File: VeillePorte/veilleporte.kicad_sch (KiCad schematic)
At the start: 0 parts

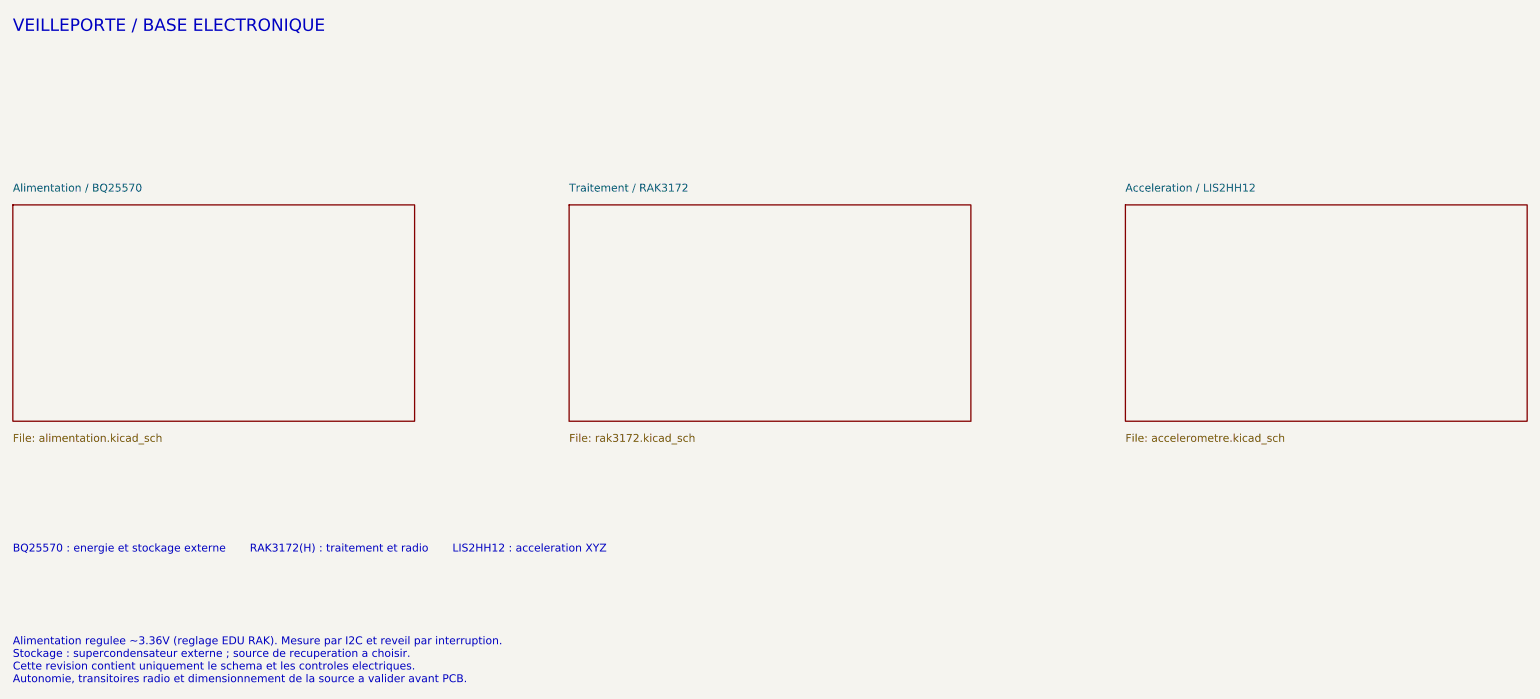
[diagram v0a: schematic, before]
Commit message: Remplace le LIS2HH12 par le raccordement IR VL53L4CD Pololu 3692
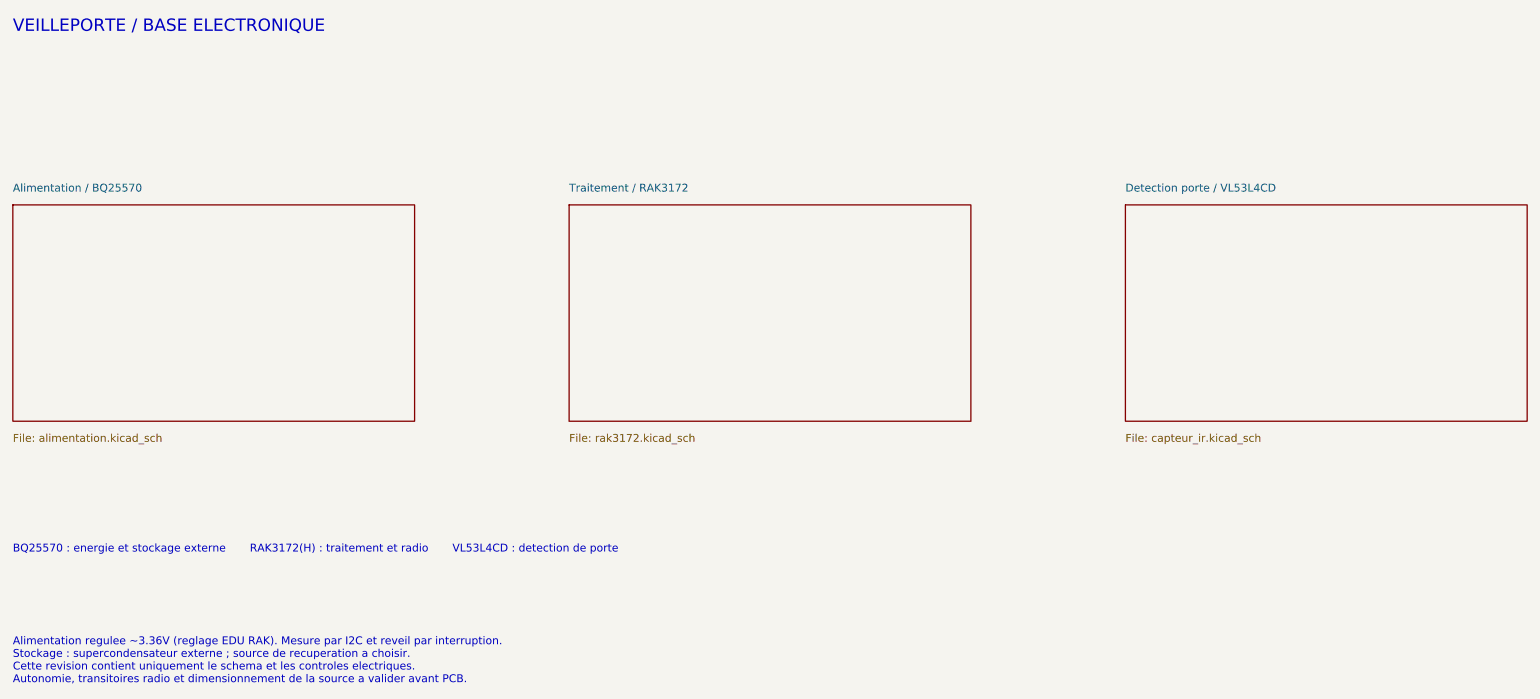
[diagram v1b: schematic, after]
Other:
- sheet Acceleration / LIS2HH12 renamed Detection porte / VL53L4CD
- sheet Detection porte / VL53L4CD: file accelerometre.kicad_sch -> capteur_ir.kicad_sch
- note added: "BQ25570 : energie et stockage externe RAK3172(H) : traitement et radio VL53L4CD : detection de porte"
- note removed: "BQ25570 : energie et stockage externe RAK3172(H) : traitement et radio LIS2HH12 : acceleration XYZ"

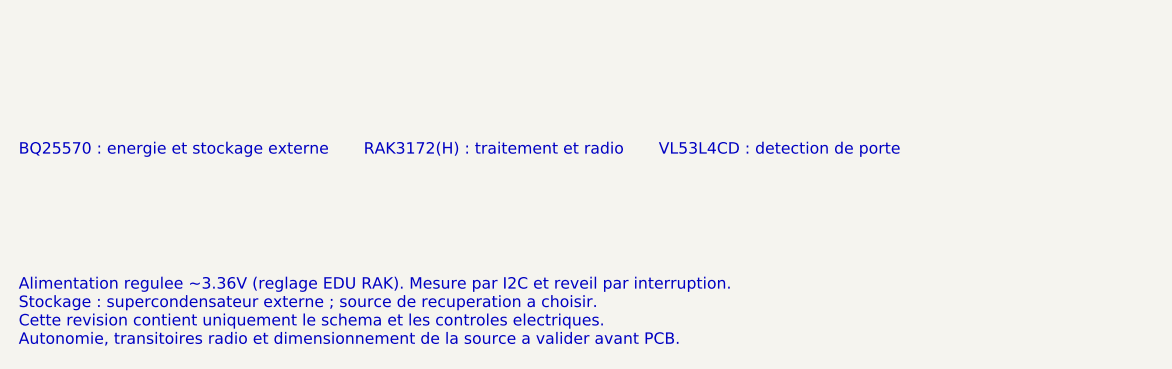
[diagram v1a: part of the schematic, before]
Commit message: Regle le BQ25570 pour supercapacite 4V et structure la feuille RAK
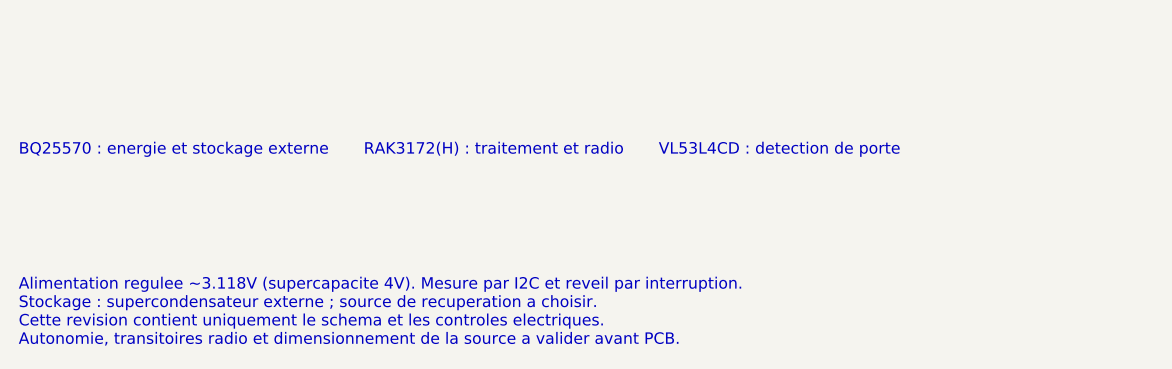
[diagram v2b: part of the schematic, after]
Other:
- note added: "Alimentation regulee ~3.118V (supercapacite 4V). Mesure par I2C et reveil par interruption. Stockage : supercondensateur externe ; source de recuperation a choisir. Cette revision contient uniquement le schema et les controles electriques. Autonomie, transitoires radio et dimensionnement de la source a valider avant PCB."
- note removed: "Alimentation regulee ~3.36V (reglage EDU RAK). Mesure par I2C et reveil par interruption. Stockage : supercondensateur externe ; source de recuperation a choisir. Cette revision contient uniquement le schema et les controles electriques. Autonomie, transitoires radio et dimensionnement de la source a valider avant PCB."
